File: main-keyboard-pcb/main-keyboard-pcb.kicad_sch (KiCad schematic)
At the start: 183 parts, among them IC1 TPS563231DRLT, J1 Debug SWD Connector, J2 Hotplug, J3 USB_B_Micro, J4 Hotplug, SW1 SW_Push, SW10 SW_Push, SW11 SW_Push, SW12 SW_Push, SW13 SW_Push, SW14 SW_Push, SW15 SW_Push, SW16 SW_Push, SW17 SW_Push, SW18 SW_Push, SW19 SW_Push, SW2 SW_Push, SW20 SW_Push, SW21 SW_Push, SW22 SW_Push, SW23 SW_Push, SW24 SW_Push, SW25 SW_Push, SW26 SW_Push, SW27 SW_Push, SW28 SW_Push, SW29 SW_Push, SW3 SW_Push, SW30 SW_Push, SW31 SW_Push, SW32 SW_Push, SW33 SW_Push, SW34 SW_Push, SW35 SW_Push, SW36 SW_Push, SW37 SW_Push, SW38 SW_Push, SW39 SW_Push, SW4 SW_Push, SW40 SW_Push, SW41 SW_Push, SW42 SW_Push, SW43 SW_Push, SW44 SW_Push, SW45 SW_Push, SW46 SW_Push, SW47 SW_Push, SW48 SW_Push, SW49 SW_Push, SW5 SW_Push, SW50 SW_Push, SW51 SW_Push, SW52 SW_Push, SW53 SW_Push, SW54 SW_Push, SW55 SW_Push, SW56 SW_Push, SW57 SW_Push, SW58 SW_Push, SW59 SW_Push, SW6 SW_Push, SW60 SW_Push, SW61 SW_Push, SW62 SW_Push, SW63 SW_Push, SW64 SW_Push, SW65 SW_Push, SW66 SW_Push, SW67 SW_Push, SW7 SW_Push, SW8 SW_Push, SW9 SW_Push, SW99 SW_SPDT, U1 USBLC6-4SC6, U2 STM32F407VGT6, Y1 16MHz

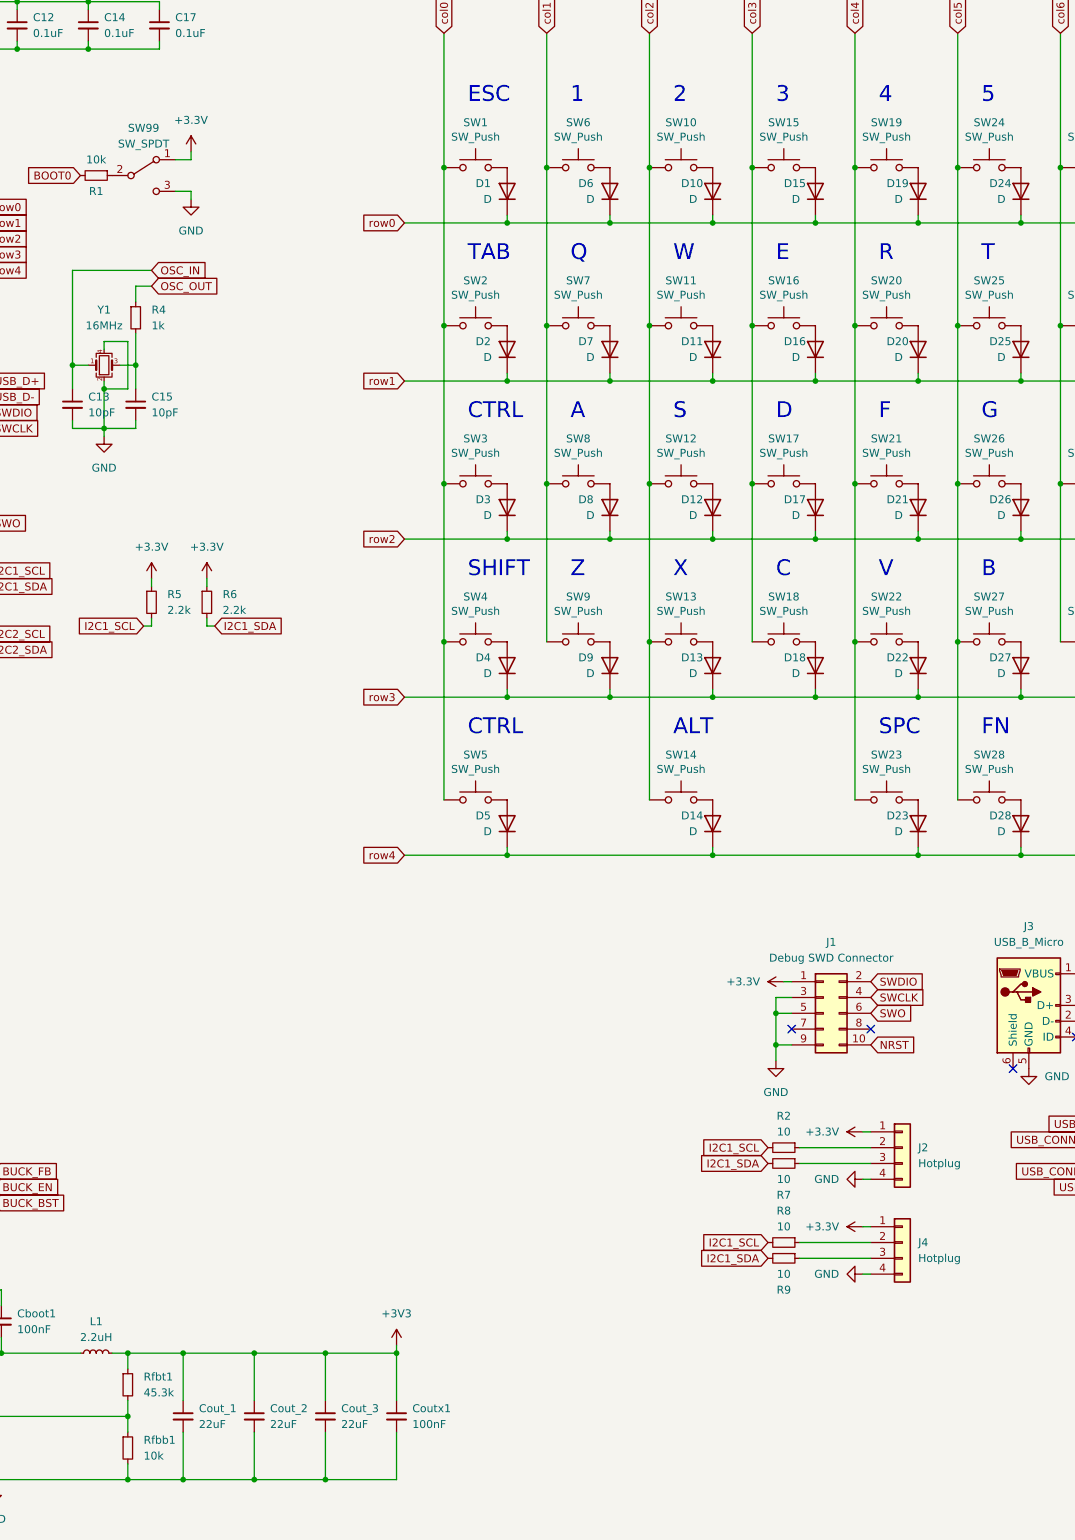
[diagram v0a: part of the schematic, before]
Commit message: Replaced Boot0 with reset sw and created exclusion zone on oscillator
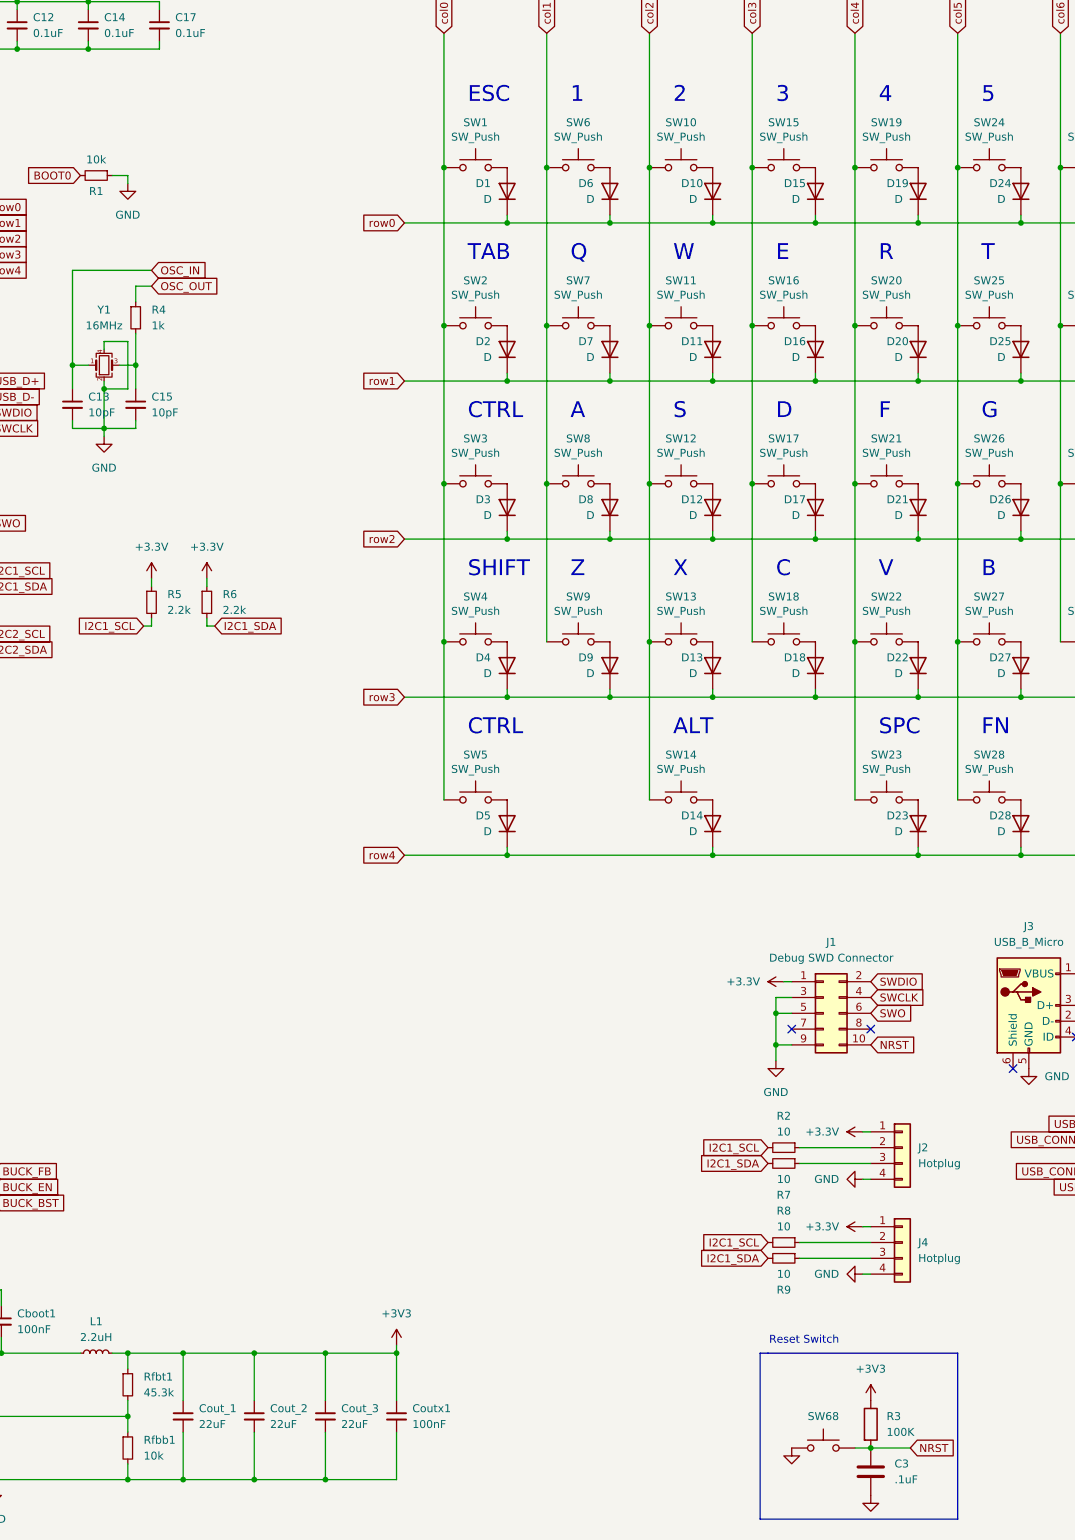
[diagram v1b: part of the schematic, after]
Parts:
- removed SW99: SW_SPDT, Button_Switch_SMD:SW_SPDT_PCM12, symbol Switch:SW_SPDT
- added C3: .1uF, stm32f4_2:C0805C104K5RAC7411, symbol Device:C
- added R3: 100K, stm32f4_2:100k, symbol Device:R
- added SW68: SW_Push, stm32f4_2:Button, symbol Switch:SW_Push
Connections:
- net +3V3: now also R3.1
- net GND: now also R1.1, C3.2, SW68.1
- net NRST: now also C3.1, R3.2, SW68.2
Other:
- note added: "Reset Switch"

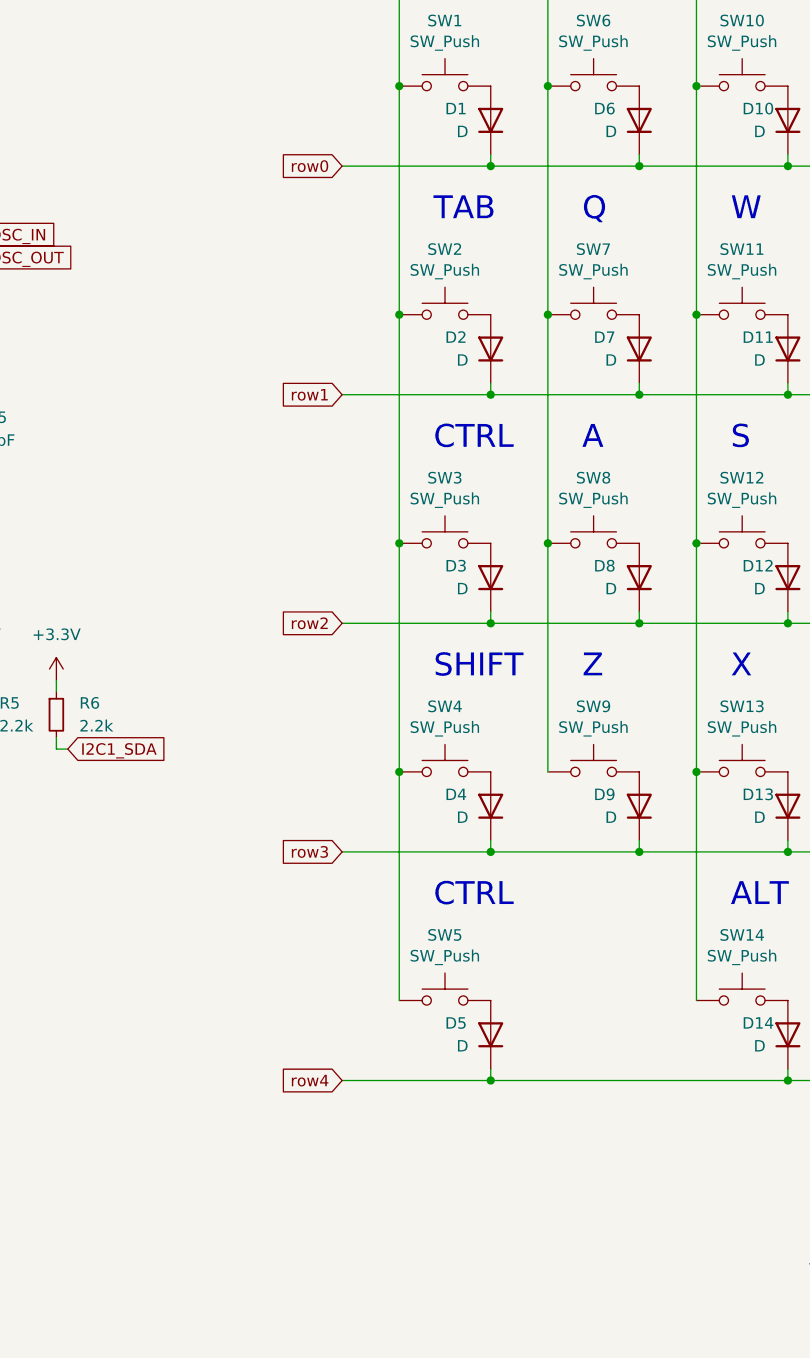
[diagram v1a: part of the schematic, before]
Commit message: Fixed osc pads and added pull down resistors
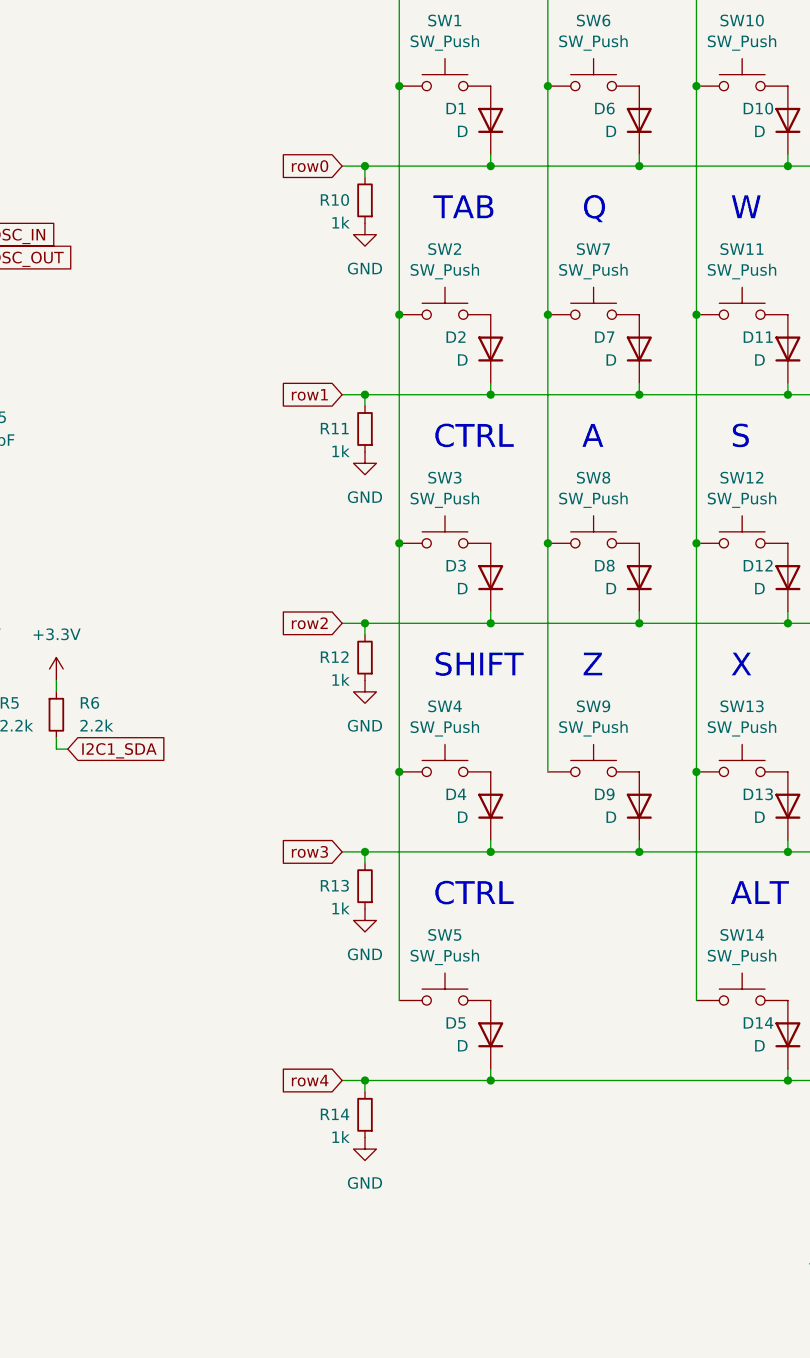
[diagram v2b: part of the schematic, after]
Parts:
- added R10, R11, R12, R13, R14: 1k, stm32f4_2:ERJ-U06F1001V, symbol Device:R_Small
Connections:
- net GND: now also R10.1, R11.1, R12.1, R13.1, R14.1
- net row0: now also R10.2
- net row1: now also R11.2
- net row2: now also R12.2
- net row3: now also R13.2
- net row4: now also R14.2

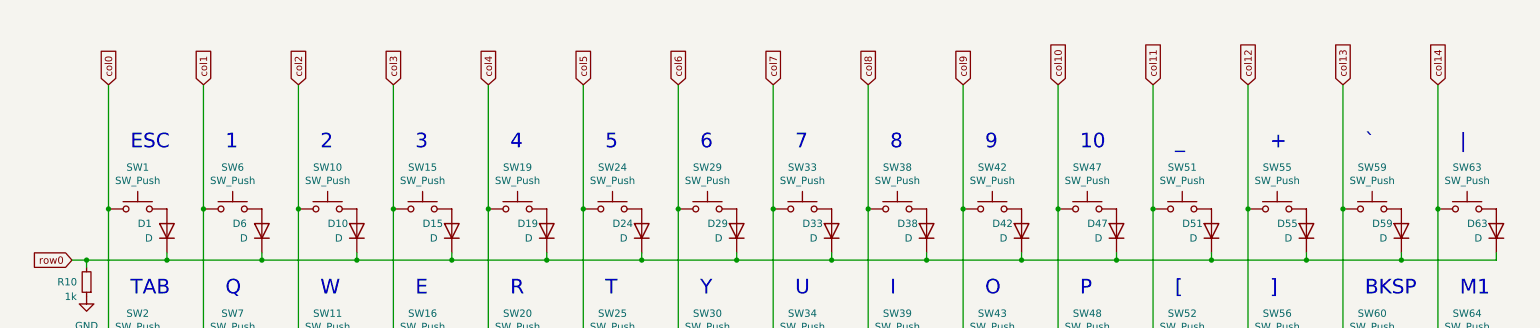
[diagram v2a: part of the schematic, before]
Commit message: added series resistors
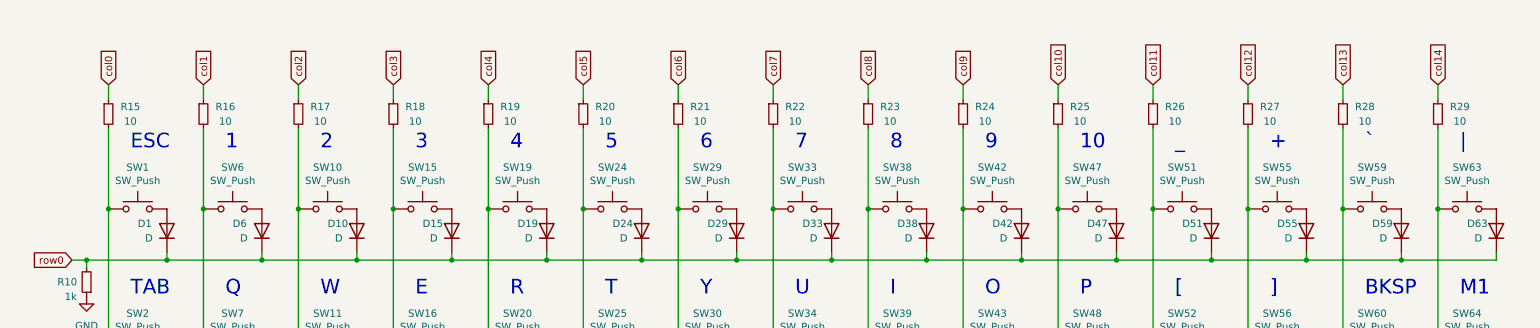
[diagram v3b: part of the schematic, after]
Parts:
- added R15, R16, R17, R18, R19, R20, R21, R22, R23, R24, R25, R26, R27, R28, R29: 10, stm32f4_2:ERJ-U06J100V, symbol Device:R_Small
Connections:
- net col0: now also R15.1; no longer SW1.1, SW2.1, SW3.1, SW4.1, SW5.1
- net col1: now also R16.1; no longer SW6.1, SW7.1, SW8.1, SW9.1
- net col10: now also R25.1; no longer SW47.1, SW48.1, SW49.1, SW50.1
- net col11: now also R26.1; no longer SW51.1, SW52.1, SW53.1, SW54.1
- net col12: now also R27.1; no longer SW55.1, SW56.1, SW57.1, SW58.1
- net col13: now also R28.1; no longer SW59.1, SW60.1, SW61.1, SW62.1
- net col14: now also R29.1; no longer SW63.1, SW64.1, SW65.1, SW66.1, SW67.1
- net col2: now also R17.1; no longer SW10.1, SW11.1, SW12.1, SW13.1, SW14.1
- net col3: now also R18.1; no longer SW15.1, SW16.1, SW17.1, SW18.1
- net col4: now also R19.1; no longer SW19.1, SW20.1, SW21.1, SW22.1, SW23.1
- net col5: now also R20.1; no longer SW24.1, SW25.1, SW26.1, SW27.1, SW28.1
- net col6: now also R21.1; no longer SW29.1, SW30.1, SW31.1, SW32.1
- net col7: now also R22.1; no longer SW33.1, SW34.1, SW35.1, SW36.1, SW37.1
- net col8: now also R23.1; no longer SW38.1, SW39.1, SW40.1, SW41.1
- net col9: now also R24.1; no longer SW42.1, SW43.1, SW44.1, SW45.1, SW46.1
- new net: R15.2, SW1.1, SW2.1, SW3.1, SW4.1, SW5.1
- new net: R17.2, SW10.1, SW11.1, SW12.1, SW13.1, SW14.1
- new net: R28.2, SW59.1, SW60.1, SW61.1, SW62.1
- new net: R18.2, SW15.1, SW16.1, SW17.1, SW18.1
- new net: R20.2, SW24.1, SW25.1, SW26.1, SW27.1, SW28.1
- new net: R23.2, SW38.1, SW39.1, SW40.1, SW41.1
- new net: R24.2, SW42.1, SW43.1, SW44.1, SW45.1, SW46.1
- new net: R21.2, SW29.1, SW30.1, SW31.1, SW32.1
- new net: R19.2, SW19.1, SW20.1, SW21.1, SW22.1, SW23.1
- new net: R27.2, SW55.1, SW56.1, SW57.1, SW58.1
- new net: R22.2, SW33.1, SW34.1, SW35.1, SW36.1, SW37.1
- new net: R29.2, SW63.1, SW64.1, SW65.1, SW66.1, SW67.1
- new net: R26.2, SW51.1, SW52.1, SW53.1, SW54.1
- new net: R25.2, SW47.1, SW48.1, SW49.1, SW50.1
- new net: R16.2, SW6.1, SW7.1, SW8.1, SW9.1
